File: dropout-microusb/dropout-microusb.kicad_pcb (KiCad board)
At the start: 2 copper layers, 75 x 94.1 mm, 45 parts, among them SW1 Rotary_Encoder_Switch, SW2 SW_Push, U1 ProMicro

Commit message: firmware
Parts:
- added C1: 10nF, Capacitor_SMD:C_0805_2012Metric_Pad1.15x1.40mm_HandSolder, B.Cu at (156.6, 60.3)
- added C2: 10nF, Capacitor_SMD:C_0805_2012Metric_Pad1.15x1.40mm_HandSolder, B.Cu at (156.6, 57.3)
- R1: value 680 -> 330
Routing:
- net ROT-B: track 26.2 -> 31.2 mm
- net ROT-A: track 27.9 -> 32.1 mm

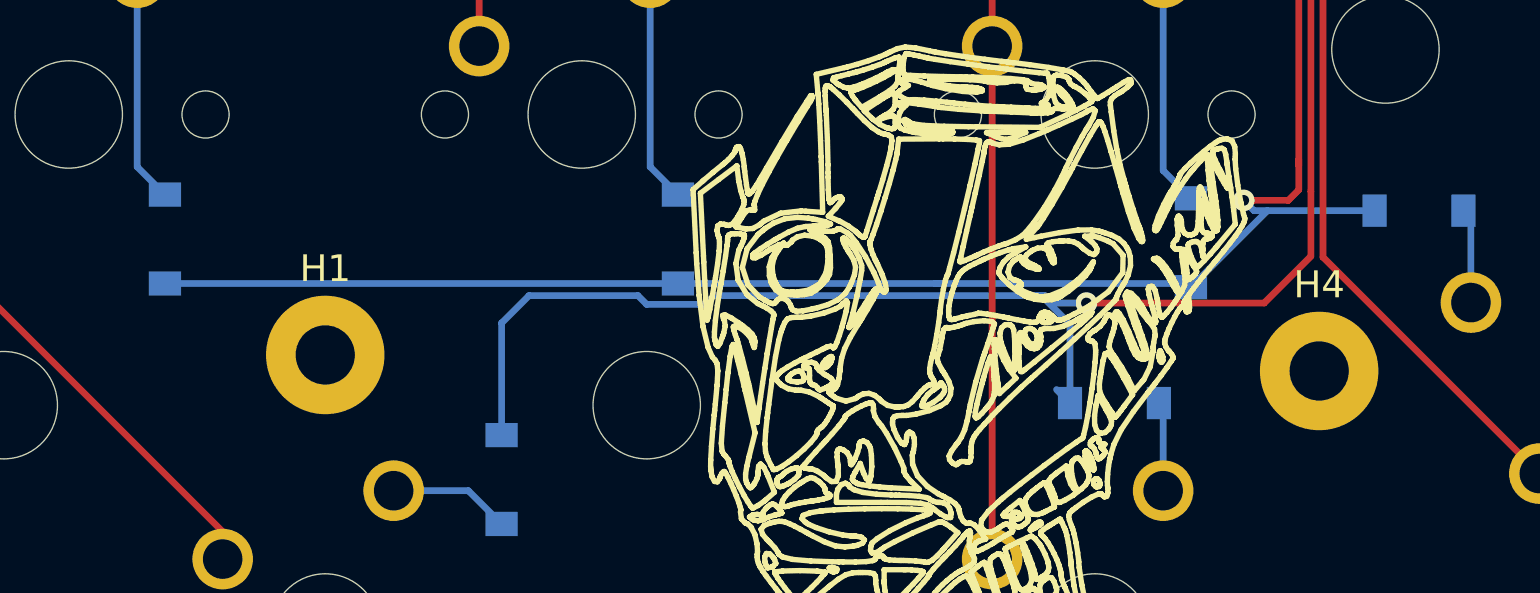
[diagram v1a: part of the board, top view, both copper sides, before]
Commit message: move screws away from stabs
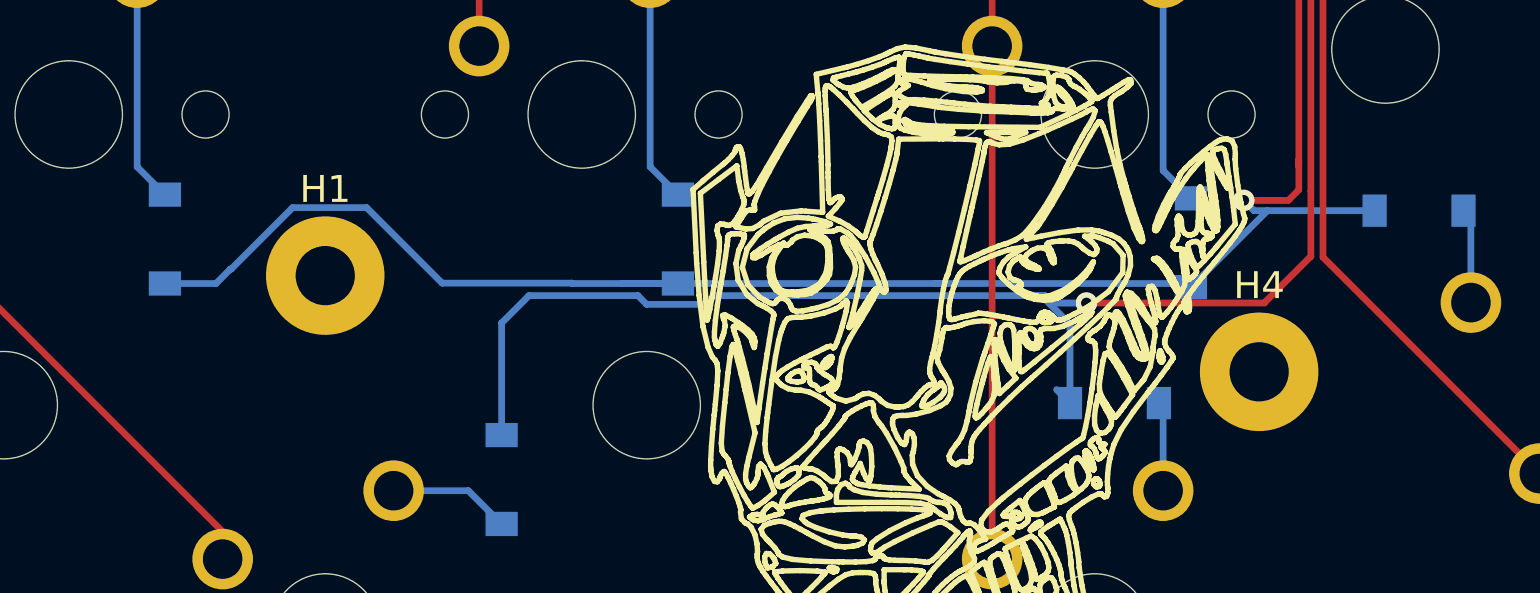
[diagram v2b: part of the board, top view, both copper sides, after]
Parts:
- moved H1 2.95 mm to (111.2, 122.8)
- moved H4 2.23 mm to (145.9, 126.4)
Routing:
- net ROW3: track 117.9 -> 123.0 mm
